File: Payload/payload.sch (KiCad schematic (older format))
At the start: 90 parts, among them J1 Conn_ARM_JTAG_SWD_10, J2 Conn_01x02, J3 Conn_01x03, Q1 Q_PMOS_DGS, Q2 Q_PMOS_DGS, SW1 SW_SPST, U1 STM32L471RGTx, U2 CY62167EV30LL-45ZXA, U3 CY62167EV30LL-45ZXA, U4 CY62167EV30LL-45ZXA, U5 CY62167EV30LL-45ZXA, Y1 8 MHz

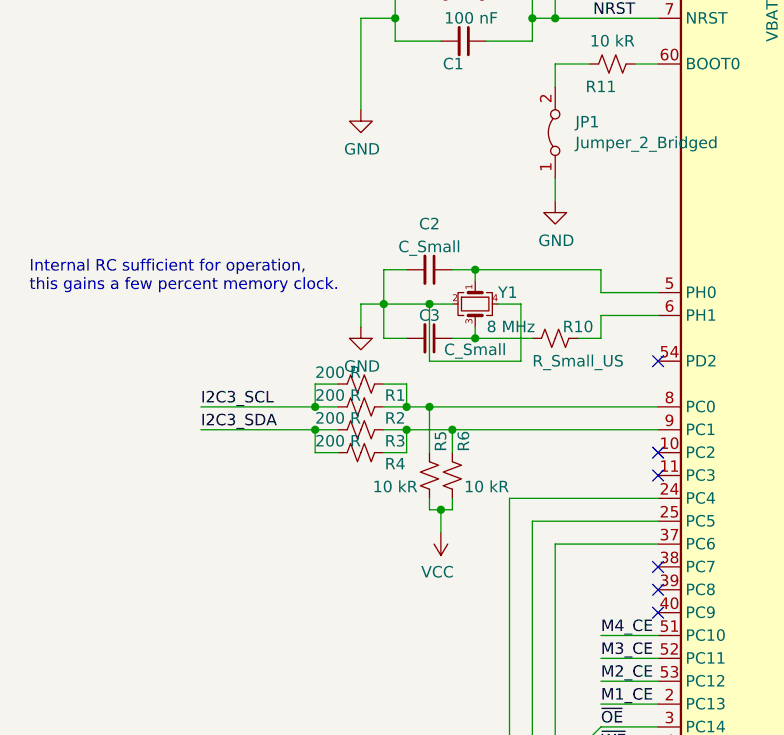
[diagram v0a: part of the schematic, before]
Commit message: Add I2C isolation
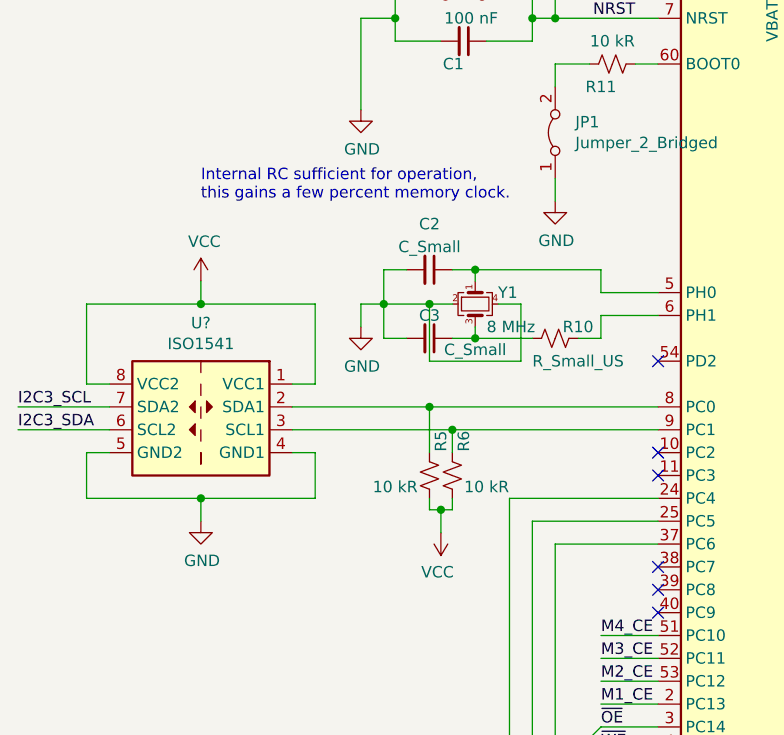
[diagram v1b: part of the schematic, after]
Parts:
- removed R1, R2, R3, R4: 200 R, symbol Device:R_Small_US
- added U?: ISO1541, Package_SO:SOIC-8_3.9x4.9mm_P1.27mm, symbol Isolator:ISO1541
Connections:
- net GND: now also U?.4 (GND1), U?.5 (GND2)
- net I2C3_SCL: now also U?.7 (SDA2)
- net I2C3_SDA: now also U?.6 (SCL2)
- net VCC: now also U?.1 (VCC1), U?.8 (VCC2)
- net at R5.2, U1.8 (PC0): now also U?.2 (SDA1)
- net at R6.2, U1.9 (PC1): now also U?.3 (SCL1)
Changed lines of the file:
@@
 	0    1    1    0
 $EndComp
-Text Label 1600 5650 0    50   ~ 0
-I2C3_SCL
-Text Label 1600 5750 0    50   ~ 0
-I2C3_SDA
 Text Label 10950 4500 0    50   ~ 0
 A0
@@
 	10200 3900 9350 3900
 Connection ~ 9350 3900
-$Comp
-L Device:R_Small_US R3
-U 1 1 6068B4BE
-P 2300 5750
-F 0 "R3" V 2250 5600 50  0000 C CNN
-F 1 "200 R" V 2250 5850 50  0000 C CNN
-F 2 "" H 2300 5750 50  0001 C CNN
-F 3 "~" H 2300 5750 50  0001 C CNN
-	1    2300 5750
-	0    -1   -1   0
-$EndComp
-$Comp
-L Device:R_Small_US R2
-U 1 1 6068B4C4
-P 2300 5650
-F 0 "R2" V 2250 5500 50  0000 C CNN
-F 1 "200 R" V 2450 5750 50  0000 C CNN
-F 2 "" H 2300 5650 50  0001 C CNN
-F 3 "~" H 2300 5650 50  0001 C CNN
-	1    2300 5650
-	0    -1   -1   0
-$EndComp
 Wire Wire Line
 	9450 6100 9350 6100
@@
 	16600 3900 16700 3900
 Connection ~ 2600 5650
-Wire Wire Line
-	2500 5750 2700 5750
 Connection ~ 2700 5750
 $Comp
@@
 	21050 3900 21050 4000
 $Comp
-L Device:R_Small_US R1
-U 1 1 61105287
-P 2300 5550
-F 0 "R1" V 2250 5400 50  0000 C CNN
-F 1 "200 R" V 2250 5650 50  0000 C CNN
-F 2 "" H 2300 5550 50  0001 C CNN
-F 3 "~" H 2300 5550 50  0001 C CNN
-	1    2300 5550
-	0    -1   -1   0
-$EndComp
-$Comp
-L Device:R_Small_US R4
-U 1 1 6110528D
-P 2300 5850
-F 0 "R4" V 2250 5700 50  0000 C CNN
-F 1 "200 R" V 2450 5950 50  0000 C CNN
-F 2 "" H 2300 5850 50  0001 C CNN
-F 3 "~" H 2300 5850 50  0001 C CNN
-	1    2300 5850
-	0    -1   -1   0
-$EndComp
-Wire Wire Line
-	2400 5650 2500 5650
-Wire Wire Line
-	2400 5550 2500 5550
-Wire Wire Line
-	2500 5550 2500 5650
-Connection ~ 2500 5650
-Wire Wire Line
-	2500 5650 2600 5650
-Wire Wire Line
-	2500 5750 2500 5850
-Wire Wire Line
-	2500 5850 2400 5850
-Wire Wire Line
-	2500 5750 2400 5750
-Connection ~ 2500 5750
-Wire Wire Line
-	1600 5650 2100 5650
-Wire Wire Line
-	1600 5750 2100 5750
-Wire Wire Line
-	2200 5550 2100 5550
-Wire Wire Line
-	2100 5550 2100 5650
-Connection ~ 2100 5650
-Wire Wire Line
-	2100 5650 2200 5650
-Wire Wire Line
-	2100 5750 2100 5850
-Wire Wire Line
-	2100 5850 2200 5850
-Connection ~ 2100 5750
-Wire Wire Line
-	2100 5750 2200 5750
-$Comp
 L Connector:Conn_ARM_JTAG_SWD_10 J1
 U 1 1 606D5873
@@
 Text Notes 21250 4000 0    50   ~ 0
 Guarantees rail -> 0 within known time
-Text Notes 850  5150 0    50   ~ 0
+Text Notes 1600 4750 0    50   ~ 0
 Internal RC sufficient for operation,\nthis gains a few percent memory clock.
 Wire Wire Line
@@
 Wire Wire Line
 	7550 5000 7550 7900
+Connection ~ 7550 5000
+Wire Wire Line
+	7550 5000 7650 5000
+$Comp
+L Isolator:ISO1541 U?
+U 1 1 60830529
+P 1600 5650
+F 0 "U?" H 1600 6017 50  0000 C CNN
+F 1 "ISO1541" H 1600 5926 50  0000 C CNN
+F 2 "Package_SO:SOIC-8_3.9x4.9mm_P1.27mm" H 1600 5300 50  0001 C CNN
+F 3 "http://www.ti.com/lit/ds/symlink/iso1541.pdf" H 1600 5700 50  0001 C CNN
+	1    1600 5650
+	-1   0    0    -1
+$EndComp
+Wire Wire Line
+	2000 5750 2700 5750
+Wire Wire Line
+	2000 5650 2600 5650
+Wire Wire Line
+	2000 5550 2100 5550
+$Comp
+L power:GND #PWR?
+U 1 1 60A7FE9C
+P 1600 6150
+F 0 "#PWR?" H 1600 5900 50  0001 C CNN
+F 1 "GND" H 1605 5977 50  0000 C CNN
+F 2 "" H 1600 6150 50  0001 C CNN
+F 3 "" H 1600 6150 50  0001 C CNN
+	1    1600 6150
+	1    0    0    -1
+$EndComp
+Wire Wire Line
+	1600 6050 1600 6150
+$Comp
+L power:VCC #PWR?
+U 1 1 60B3F22B
+P 1600 5100
+F 0 "#PWR?" H 1600 4950 50  0001 C CNN
+F 1 "VCC" H 1615 5273 50  0000 C CNN
+F 2 "" H 1600 5100 50  0001 C CNN
+F 3 "" H 1600 5100 50  0001 C CNN
+	1    1600 5100
+	1    0    0    -1
+$EndComp
+Text Label 800  5650 0    50   ~ 0
+I2C3_SCL
+Text Label 800  5750 0    50   ~ 0
+I2C3_SDA
+Wire Wire Line
+	800  5750 1200 5750
+Wire Wire Line
+	1200 5650 800  5650
+Wire Wire Line
+	2100 5550 2100 5200
+Wire Wire Line
+	2100 5200 1600 5200
+Wire Wire Line
+	1600 5200 1600 5100
+Wire Wire Line
+	1600 5200 1100 5200
+Wire Wire Line
+	1100 5200 1100 5550
+Wire Wire Line
+	1100 5550 1200 5550
+Connection ~ 1600 5200
+Wire Wire Line
+	2000 5850 2100 5850
+Wire Wire Line
+	2100 5850 2100 6050
+Wire Wire Line
+	2100 6050 1600 6050
+Wire Wire Line
+	1200 5850 1100 5850
+Wire Wire Line
+	1100 5850 1100 6050
+Wire Wire Line
+	1100 6050 1600 6050
 Wire Bus Line
 	18700 5000 18700 7750
@@
 Wire Bus Line
 	20750 4600 20750 7450
-Connection ~ 7550 5000
-Wire Wire Line
-	7550 5000 7650 5000
+Connection ~ 1600 6050
 $EndSCHEMATC

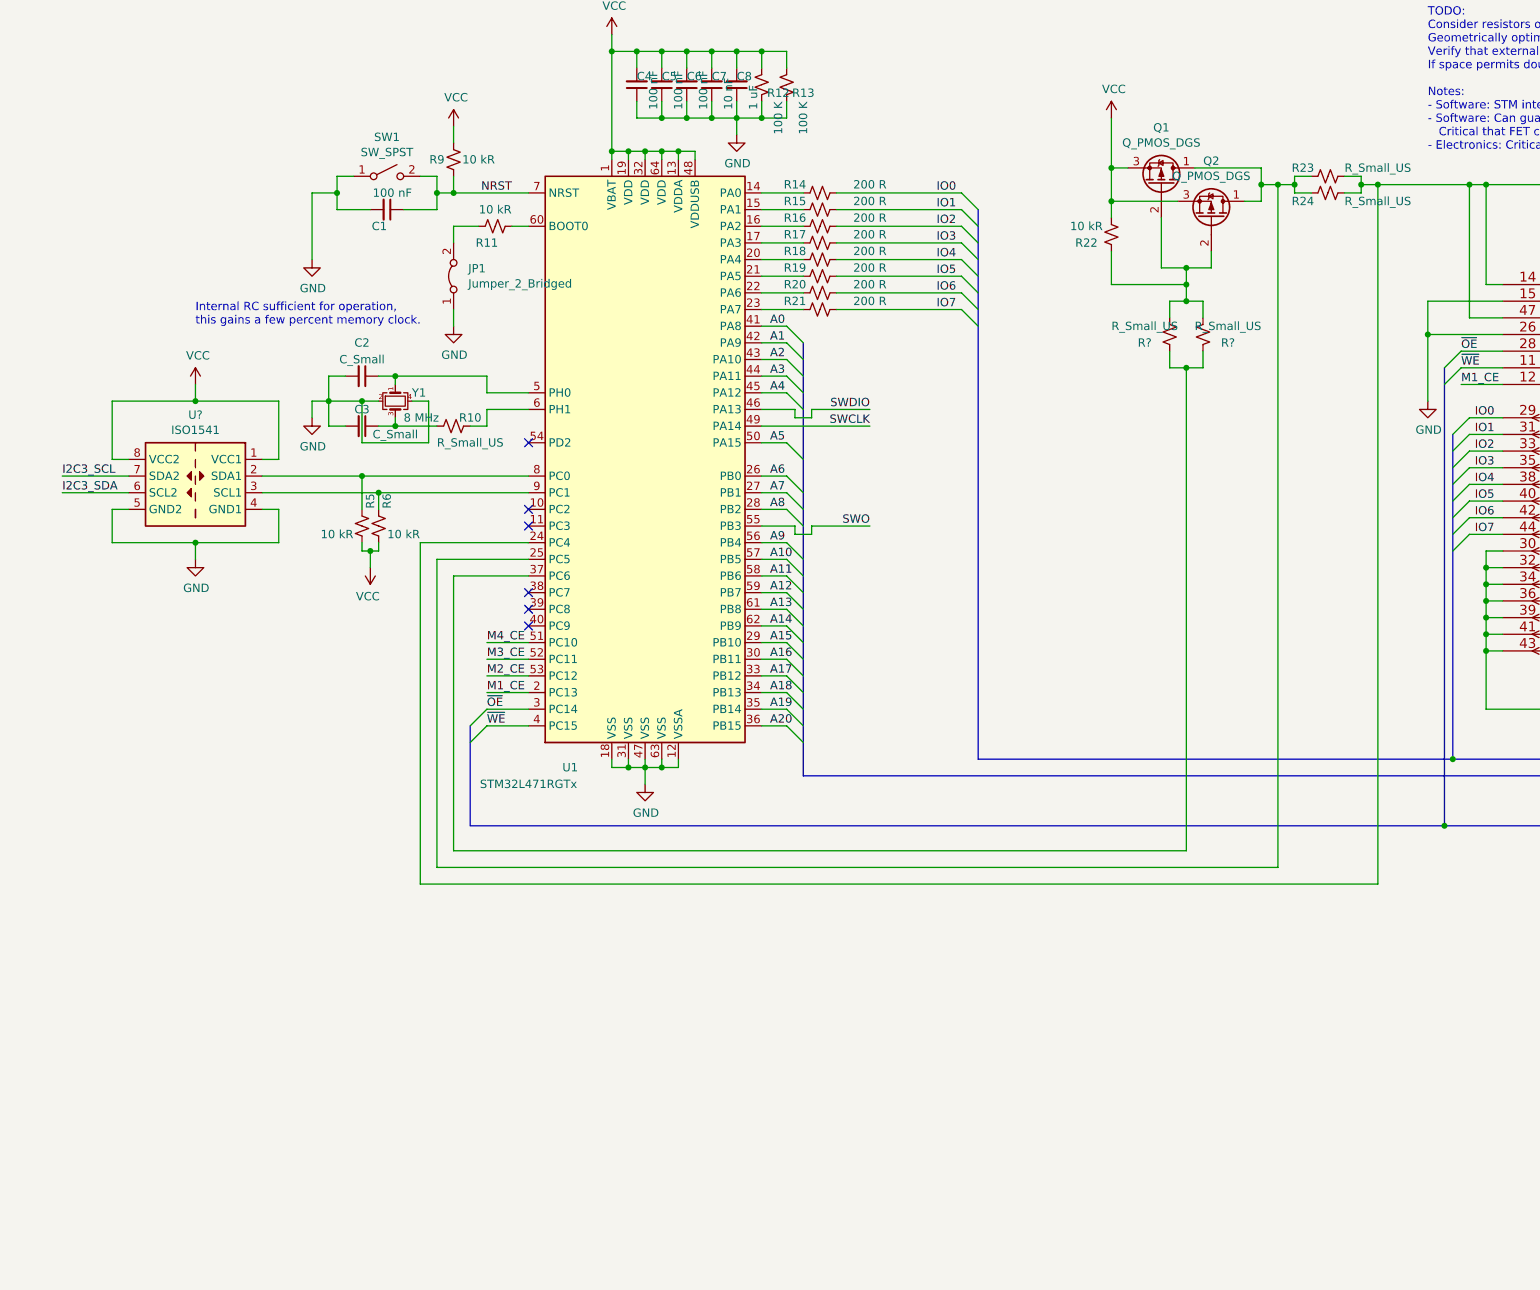
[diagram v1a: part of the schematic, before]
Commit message: Add watchdog and I2C isolator
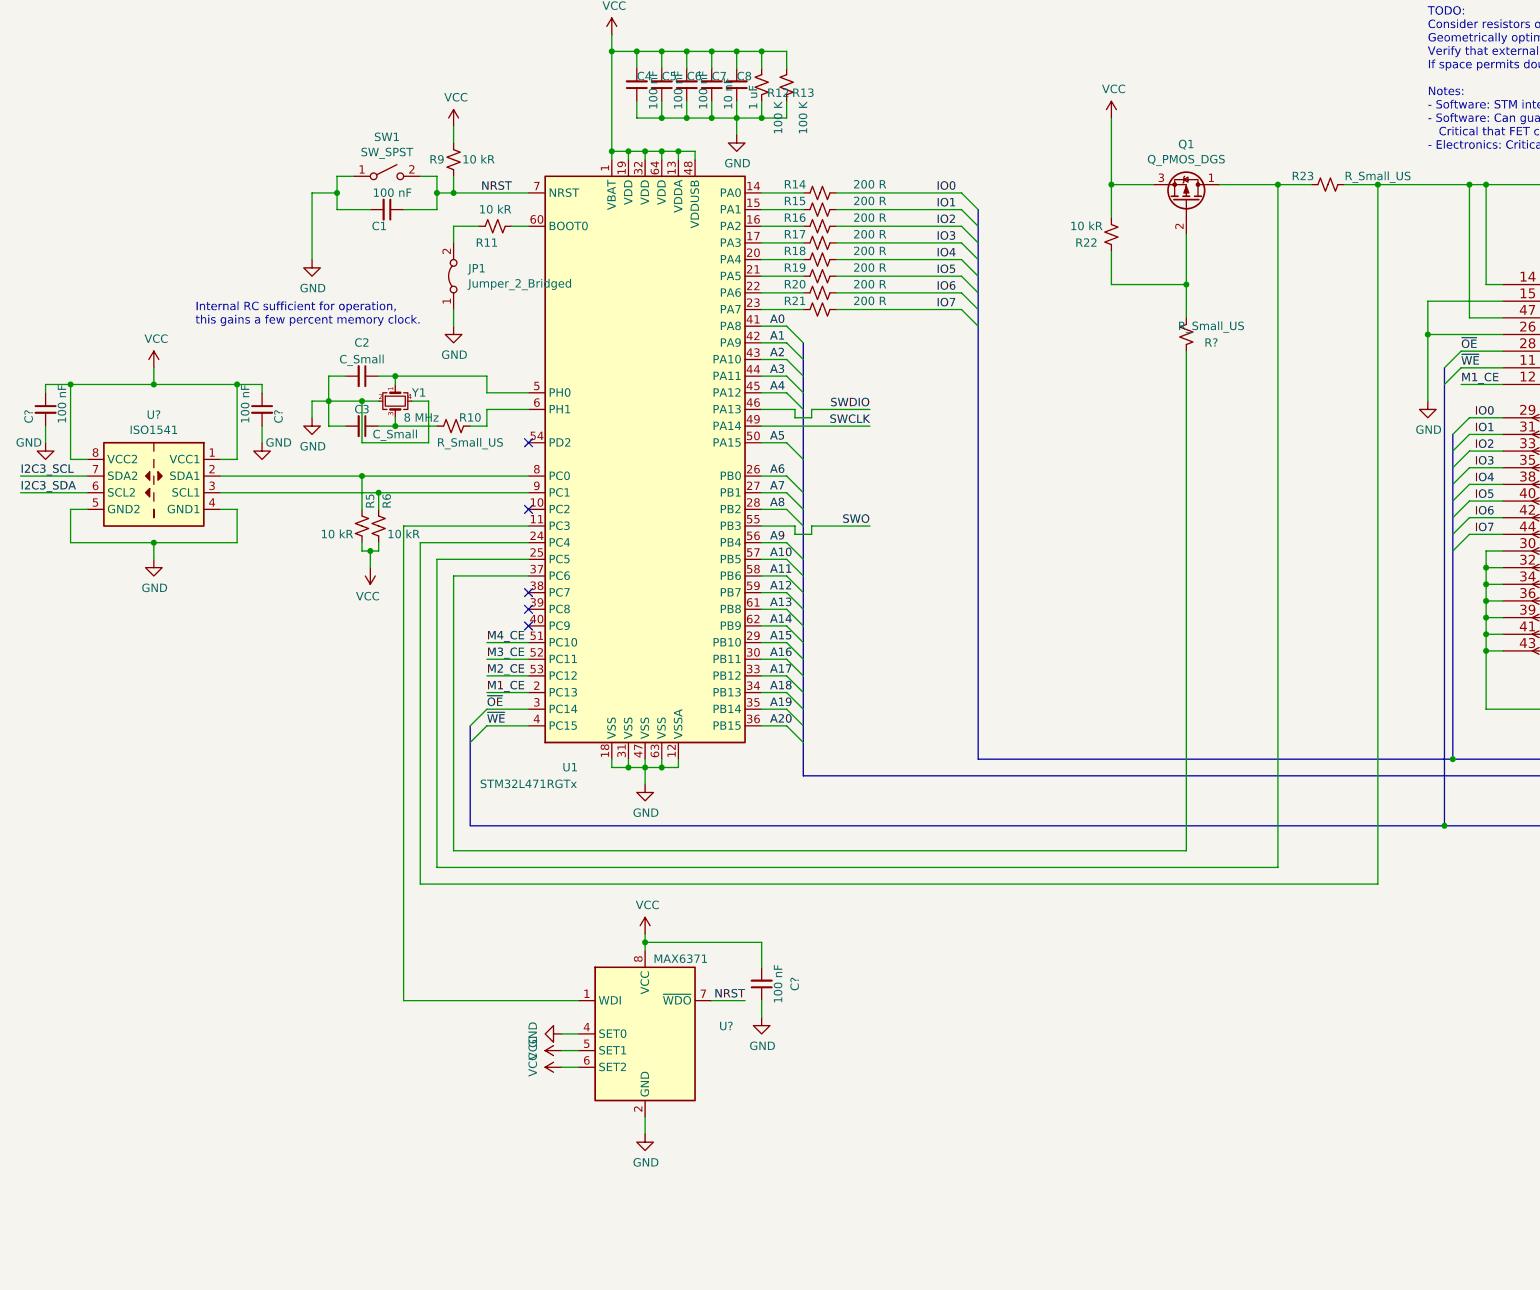
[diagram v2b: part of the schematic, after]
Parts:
- removed Q2: Q_PMOS_DGS, symbol Device:Q_PMOS_DGS
- removed R24, R?: R_Small_US, symbol Device:R_Small_US
- added C? (x3): 100 nF, symbol Device:C_Small
- added U?: MAX6371, Package_TO_SOT_SMD:SOT-23-8, symbol Power_Supervisor:MAX6371
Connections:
- net GND: now also C?.1, C?.2, C?.2, U?.2 (GND), U?.4 (SET0)
- net NRST: now also U?.7 (~WDO)
- net VCC: now also C?.1, C?.1, C?.2, U?.5 (SET1), U?.6 (SET2), U?.8 (VCC)
- net at U1.11 (PC3): now also U?.1 (WDI)
- no-connect marks 7 -> 6
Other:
- moved on the sheet: Q1, R23, R?, U?

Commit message: Replace old memory symbol
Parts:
- removed C? (x3): 100 nF, symbol Device:C_Small
- removed R26: 100 kR, symbol Device:R_Small_US
- removed U2, U3, U4, U5: CY62167EV30LL-45ZXA, TSOP-48, symbol Payload2:CY62167EV30LL-45ZXA
- added C? (x5): 100 nF, symbol Device:C_Small
- added U? (x6): CY62167EV30LL, Package_SO:TSOP-I-48_18.4x12mm_P0.5mm, symbol Payload2:CY62167EV30LL
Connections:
- net A0: now also U?.25 (A0), U?.25 (A0), U?.25 (A0), U?.25 (A0), U?.25 (A0), U?.25 (A0)
- net A1: now also U?.24 (A1), U?.24 (A1), U?.24 (A1), U?.24 (A1), U?.24 (A1), U?.24 (A1)
- net A10: now also U?.6 (A10), U?.6 (A10), U?.6 (A10), U?.6 (A10), U?.6 (A10), U?.6 (A10)
- net A11: now also U?.5 (A11), U?.5 (A11), U?.5 (A11), U?.5 (A11), U?.5 (A11), U?.5 (A11)
- net A12: now also U?.4 (A12), U?.4 (A12), U?.4 (A12), U?.4 (A12), U?.4 (A12), U?.4 (A12)
- net A13: now also U?.3 (A13), U?.3 (A13), U?.3 (A13), U?.3 (A13), U?.3 (A13), U?.3 (A13)
- net A14: now also U?.2 (A14), U?.2 (A14), U?.2 (A14), U?.2 (A14), U?.2 (A14), U?.2 (A14)
- net A15: now also U?.1 (A15), U?.1 (A15), U?.1 (A15), U?.1 (A15), U?.1 (A15), U?.1 (A15)
- net A16: now also U?.48 (A16), U?.48 (A16), U?.48 (A16), U?.48 (A16), U?.48 (A16), U?.48 (A16)
- net A17: now also U?.17 (A17), U?.17 (A17), U?.17 (A17), U?.17 (A17), U?.17 (A17), U?.17 (A17)
- net A18: now also U?.16 (A18), U?.16 (A18), U?.16 (A18), U?.16 (A18), U?.16 (A18), U?.16 (A18)
- net A19: now also U?.9 (A19), U?.9 (A19), U?.9 (A19), U?.9 (A19), U?.9 (A19), U?.9 (A19)
- net A2: now also U?.23 (A2), U?.23 (A2), U?.23 (A2), U?.23 (A2), U?.23 (A2), U?.23 (A2)
- net A20: now also U?.45 (IO15/A20), U?.45 (IO15/A20), U?.45 (IO15/A20), U?.45 (IO15/A20), U?.45 (IO15/A20), U?.45 (IO15/A20)
- net A3: now also U?.22 (A3), U?.22 (A3), U?.22 (A3), U?.22 (A3), U?.22 (A3), U?.22 (A3)
- net A4: now also U?.21 (A4), U?.21 (A4), U?.21 (A4), U?.21 (A4), U?.21 (A4), U?.21 (A4)
- net A5: now also U?.20 (A5), U?.20 (A5), U?.20 (A5), U?.20 (A5), U?.20 (A5), U?.20 (A5)
- net A6: now also U?.19 (A6), U?.19 (A6), U?.19 (A6), U?.19 (A6), U?.19 (A6), U?.19 (A6)
- net A7: now also U?.18 (A7), U?.18 (A7), U?.18 (A7), U?.18 (A7), U?.18 (A7), U?.18 (A7)
- net A8: now also U?.8 (A8), U?.8 (A8), U?.8 (A8), U?.8 (A8), U?.8 (A8), U?.8 (A8)
- net A9: now also U?.7 (A9), U?.7 (A9), U?.7 (A9), U?.7 (A9), U?.7 (A9), U?.7 (A9)
- net GND: now also C?.1, C?.1, C?.1, C?.1, C?.1, U?.11 (~WE), U?.11 (~WE), U?.11 (~WE), U?.11 (~WE), U?.11 (~WE), U?.11 (~WE), U?.12 (CE2), U?.12 (CE2), U?.12 (CE2), U?.12 (CE2), U?.12 (CE2), U?.12 (CE2), U?.27 (VSS), U?.27 (VSS), U?.27 (VSS), U?.27 (VSS), U?.27 (VSS), U?.27 (VSS), U?.30 (IO8), U?.30 (IO8), U?.30 (IO8), U?.30 (IO8), U?.30 (IO8), U?.30 (IO8), U?.32 (IO9), U?.32 (IO9), U?.32 (IO9), U?.32 (IO9), U?.32 (IO9), U?.32 (IO9), U?.34 (IO10), U?.34 (IO10), U?.34 (IO10), U?.34 (IO10), U?.34 (IO10), U?.34 (IO10), U?.36 (IO11), U?.36 (IO11), U?.36 (IO11), U?.36 (IO11), U?.36 (IO11), U?.36 (IO11), U?.39 (IO12), U?.39 (IO12), U?.39 (IO12), U?.39 (IO12), U?.39 (IO12), U?.39 (IO12), U?.41 (IO13), U?.41 (IO13), U?.41 (IO13), U?.41 (IO13), U?.41 (IO13), U?.41 (IO13), U?.43 (IO14), U?.43 (IO14), U?.43 (IO14), U?.43 (IO14), U?.43 (IO14), U?.43 (IO14), U?.46 (VSS), U?.46 (VSS), U?.46 (VSS), U?.46 (VSS), U?.46 (VSS), U?.46 (VSS)
- net IO0: now also U?.29 (IO0), U?.29 (IO0), U?.29 (IO0), U?.29 (IO0), U?.29 (IO0), U?.29 (IO0)
- net IO1: now also U?.31 (IO1), U?.31 (IO1), U?.31 (IO1), U?.31 (IO1), U?.31 (IO1), U?.31 (IO1)
- net IO2: now also U?.33 (IO2), U?.33 (IO2), U?.33 (IO2), U?.33 (IO2), U?.33 (IO2), U?.33 (IO2)
- net IO3: now also U?.35 (IO3), U?.35 (IO3), U?.35 (IO3), U?.35 (IO3), U?.35 (IO3), U?.35 (IO3)
- net IO4: now also U?.38 (IO4), U?.38 (IO4), U?.38 (IO4), U?.38 (IO4), U?.38 (IO4), U?.38 (IO4)
- net IO5: now also U?.40 (IO5), U?.40 (IO5), U?.40 (IO5), U?.40 (IO5), U?.40 (IO5), U?.40 (IO5)
- net IO6: now also U?.42 (IO6), U?.42 (IO6), U?.42 (IO6), U?.42 (IO6), U?.42 (IO6), U?.42 (IO6)
- net IO7: now also U?.44 (IO7), U?.44 (IO7), U?.44 (IO7), U?.44 (IO7), U?.44 (IO7), U?.44 (IO7)
- net M1_CE: now also U?.14 (~BHE), U?.14 (~BHE), U?.14 (~BHE), U?.14 (~BHE), U?.14 (~BHE), U?.14 (~BHE)
- net ~OE: now also U?.28 (~OE), U?.28 (~OE), U?.28 (~OE), U?.28 (~OE), U?.28 (~OE), U?.28 (~OE)
- net ~WE: now also U?.15 (~BLE), U?.15 (~BLE), U?.15 (~BLE), U?.15 (~BLE), U?.15 (~BLE), U?.15 (~BLE)
- net at C9.2, R23.2, R25.1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: now also C?.2, C?.2, C?.2, C?.2, C?.2, U?.26 (~CE1), U?.26 (~CE1), U?.26 (~CE1), U?.26 (~CE1), U?.26 (~CE1), U?.26 (~CE1), U?.37 (VCC), U?.37 (VCC), U?.37 (VCC), U?.37 (VCC), U?.37 (VCC), U?.37 (VCC), U?.47 (~BYTE), U?.47 (~BYTE), U?.47 (~BYTE), U?.47 (~BYTE), U?.47 (~BYTE), U?.47 (~BYTE)
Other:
- moved on the sheet: J1, J2, J3, R25, R7, R8, TP1, TP10, TP11, TP12, TP13, TP14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

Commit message: Cosmetic changes
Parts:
- removed R7: 55 R, symbol Device:R_Small_US
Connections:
- net M1_CE: no longer U?.14 (~BHE), U?.14 (~BHE), U?.14 (~BHE), U?.14 (~BHE), U?.14 (~BHE)
- net M2_CE: now also U?.14 (~BHE)
- net M3_CE: now also U?.14 (~BHE)
- net M4_CE: now also U?.14 (~BHE)
- net at U1.8 (PC0), U?.2 (SDA1): now also R6.2; no longer R5.2
- net at U1.9 (PC1), U?.3 (SCL1): now also R5.2; no longer R6.2
- new net M5_CE: U?.14 (~BHE)
- new net M6_CE: U?.14 (~BHE)
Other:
- moved on the sheet: C1, C2, C3, C4, C5, C6, C7, C8, C9, C?, J1, J2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

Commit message: Assign footprints
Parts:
- removed Q1: Q_PMOS_DGS, symbol Device:Q_PMOS_DGS
- added Q1: Q_PMOS_GSD, Resistor_SMD:R_0603_1608Metric, symbol Device:Q_PMOS_GSD
- C1, C2, C3, C4, C5, C6, C7, C8, C9: footprint (none) -> Capacitor_SMD:C_0603_1608Metric
- C10, C11, C12, C13, C14, C15, C16, C17: renamed from C?; footprint (none) -> Capacitor_SMD:C_0603_1608Metric
- J1: footprint (none) -> Connector_PinHeader_1.27mm:PinHeader_2x05_P1.27mm_Vertical
- J2: footprint (none) -> Connector_Wire:SolderWire-0.75sqmm_1x02_P7mm_D1.25mm_OD3.5mm_Relief
- J3: footprint (none) -> Connector_Wire:SolderWire-0.75sqmm_1x03_P4.8mm_D1.25mm_OD2.3mm_Relief
- JP1: footprint (none) -> Jumper:SolderJumper-2_P1.3mm_Bridged2Bar_RoundedPad1.0x1.5mm
- R1: renamed from R?; footprint (none) -> Resistor_SMD:R_0603_1608Metric
- R10, R11, R12, R13, R14, R15, R16, R17, R18, R19, R20, R21, R22, R23, R25, R5, R6, R8, R9: footprint (none) -> Resistor_SMD:R_0603_1608Metric
- SW1: footprint (none) -> Button_Switch_SMD:SW_SPST_PTS810
- TP1, TP10, TP11, TP12, TP13, TP14, TP15, TP16, TP17, TP18, TP19, TP2, TP20, TP21, TP22, TP23, TP24, TP25, TP26, TP27, TP28, TP29, TP3, TP30, TP31, TP32, TP33, TP34, TP35, TP36, TP37, TP4, TP5, TP6, TP7, TP8, TP9: footprint (none) -> TestPoint:TestPoint_Pad_1.0x1.0mm
- Y1: footprint (none) -> Payload2:Crystal_SMD_DiodesIncorporated_FY
- gave numbers to parts that had none: 8
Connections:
- net VCC: now also Q1.2 (S)
- net at R23.1, U1.25 (PC5): now also Q1.3 (D)
- net at R1.2, R22.1: now also Q1.1 (G)
